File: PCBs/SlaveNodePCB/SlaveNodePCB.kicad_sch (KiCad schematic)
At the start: 0 parts

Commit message: Designed Slave PCB schematic
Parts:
- added C1: 10uF 50v, Capacitor_SMD:C_0805_2012Metric, symbol Device:C
- added C10, C7: 0.1uF, Capacitor_SMD:C_0805_2012Metric, symbol Device:C
- added C2: 22uF 6.3V, Capacitor_SMD:C_0805_2012Metric, symbol Device:C
- added C3: 150pF, Capacitor_SMD:C_0805_2012Metric, symbol Device:C
- added C4: 100nF, Capacitor_SMD:C_0805_2012Metric, symbol Device:C
- added C5, C6, C9: 1uF, Capacitor_SMD:C_0805_2012Metric, symbol Device:C
- added D1: ~, Capacitor_SMD:C_0805_2012Metric, symbol Device:D_Schottky_Small
- added D2: FR107/1N4007, Diode_THT:D_DO-41_SOD81_P12.70mm_Horizontal, symbol Device:D
- added J1: 8P8C, Connector_RJ:RJ45_Ninigi_GE, symbol Connector:8P8C
- added J2: Screw_Terminal_01x02, TerminalBlock_Phoenix:TerminalBlock_Phoenix_PTSM-0,5-2-2,5-V-SMD_1x02-1MP_P2.50mm_Vertical, symbol Connector:Screw_Terminal_01x02
- added J3: Conn_01x04, Connector_PinHeader_2.54mm:PinHeader_1x04_P2.54mm_Vertical, symbol Connector_Generic:Conn_01x04
- added J4: Conn_01x07, Connector_PinHeader_2.54mm:PinHeader_1x07_P2.54mm_Vertical, symbol Connector_Generic:Conn_01x07
- added L1: 15uH, Inductor_SMD:L_6.3x6.3_H3, symbol Device:L
- added MP1584EN1: ~, Package_SO:SO-8_3.9x4.9mm_P1.27mm, symbol PersonalLibrary:MP1584EN
- added Q1: IRLZ44N, Package_TO_SOT_THT:TO-220-3_Vertical, symbol Transistor_FET:IRLZ44N
- added R1: 210k, Resistor_SMD:R_0805_2012Metric, symbol Device:R_Small_US
- added R2: 40.2k, Resistor_SMD:R_0805_2012Metric, symbol Device:R_Small_US
- added R3, R4, R5: 100k, Resistor_SMD:R_0805_2012Metric, symbol Device:R_Small_US
- added R6: 10K, Resistor_SMD:R_0805_2012Metric, symbol Device:R
- added SW1: RST, Button_Switch_THT:SW_PUSH_6mm, symbol Switch:SW_SPST
- added U1: AP2112K-3.3, Package_TO_SOT_SMD:SOT-23-5, symbol Regulator_Linear:AP2112K-3.3
- added U2: MAX485E, Package_SO:SOIC-8_3.9x4.9mm_P1.27mm, symbol Interface_UART:MAX485E
- added U3: STM8S003F3P, Package_SO:TSSOP-20_4.4x6.5mm_P0.65mm, symbol MCU_ST_STM8:STM8S003F3P
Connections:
- new net: C9.1, U3.8 (VCAP)
- new net: MP1584EN1.6 (FREQ), R4.1
- new net: J2.1 (Pin_1), Q1.2 (D)
- new net: C4.2, D1.1 (K), L1.1, MP1584EN1.1 (SW)
- new net: MP1584EN1.2 (EN), R5.2
- new net: C3.1, MP1584EN1.3 (COMP)
- new net: MP1584EN1.4 (FB), R1.1, R2.1
- new net: C4.1, MP1584EN1.8 (BST)
- new net: C3.2, R3.2
- new net +24V: C1.2, D2.1 (K), J1.6, J1.7, J1.8, J2.2 (Pin_2), MP1584EN1.7 (VIN), R5.1
- new net +3.3V: C10.2, C6.1, J3.1 (Pin_1), U1.5 (VOUT), U3.9 (VDD)
- new net +5V: C2.2, C5.1, J4.7 (Pin_7), L1.2, R1.2, R6.1, U1.1 (VIN), U1.3 (EN), U2.8 (VCC)
- new net 485_EN: U2.2 (~{RE}), U2.3 (DE), U3.1 (PD4)
- new net A485: J1.1, U2.6 (A)
- new net A_IN: J4.1 (Pin_1), U3.12 (PB4)
- new net B485: J1.2, U2.7 (B)
- new net GND: C1.1, C10.1, C2.1, C5.2, C6.2, C7.2, C9.2, D1.2 (A), D2.2 (A), J1.3, J1.4, J1.5, J3.2 (Pin_2), J4.6 (Pin_6), MP1584EN1.5 (GND), Q1.3 (S), R2.2, R3.1, R4.2, SW1.1 (A), U1.2 (GND), U2.5 (GND), U3.7 (VSS)
- new net NRST: C7.1, J3.3 (Pin_3), R6.2, SW1.2 (B)
- new net S0: J4.2 (Pin_2), U3.14 (PC4)
- new net S1: J4.3 (Pin_3), U3.15 (PC5)
- new net S2: J4.4 (Pin_4), U3.16 (PC6)
- new net S3: J4.5 (Pin_5), U3.17 (PC7)
- new net SV_SIGNAL: Q1.1 (G), U3.19 (PD2)
- new net SWIM: J3.4 (Pin_4), U3.18 (PD1)
- new net UART_RX: U2.1 (RO), U3.3 (PD6)
- new net UART_TX: U2.4 (DI), U3.2 (PD5)
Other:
- note added: "24V->5V Step Down Switching Regulator"
- note added: "3.3V Fixed LDO"
- note added: "Input Connector"
- note added: "MAX485"
- note added: "Mux Connect"
- note added: "Program"
- note added: "Reset"
- note added: "STM8S003F3"
- note added: "Solenoid Valve Output"

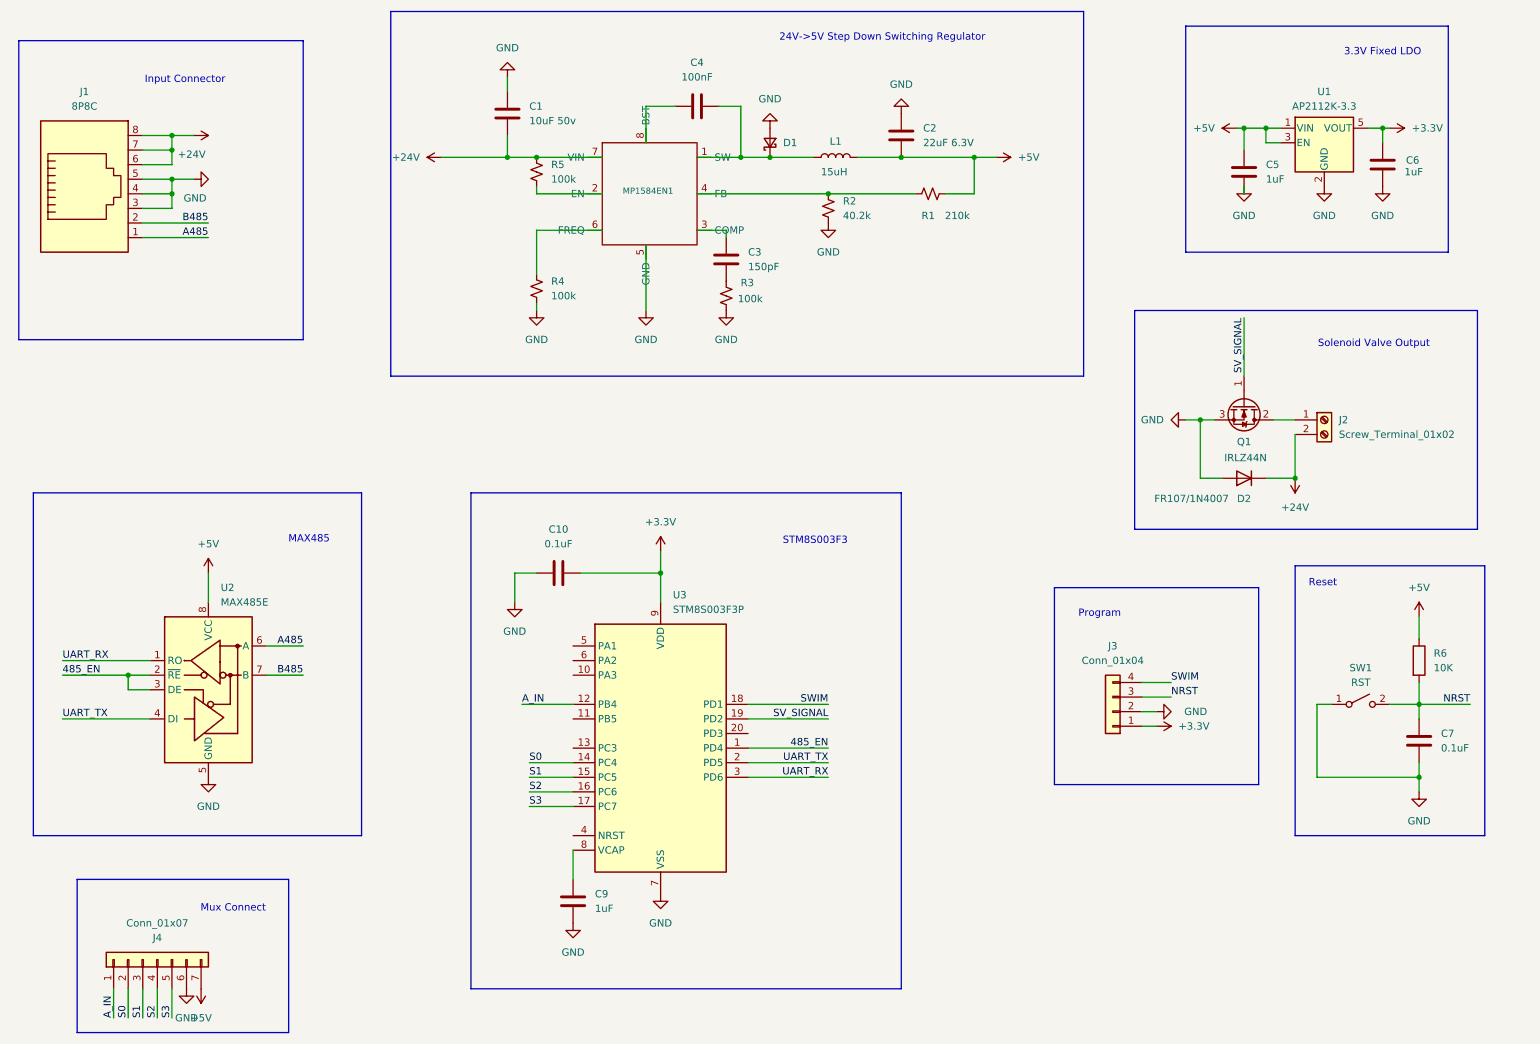
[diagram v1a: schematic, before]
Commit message: First Slave PCB Design Complete
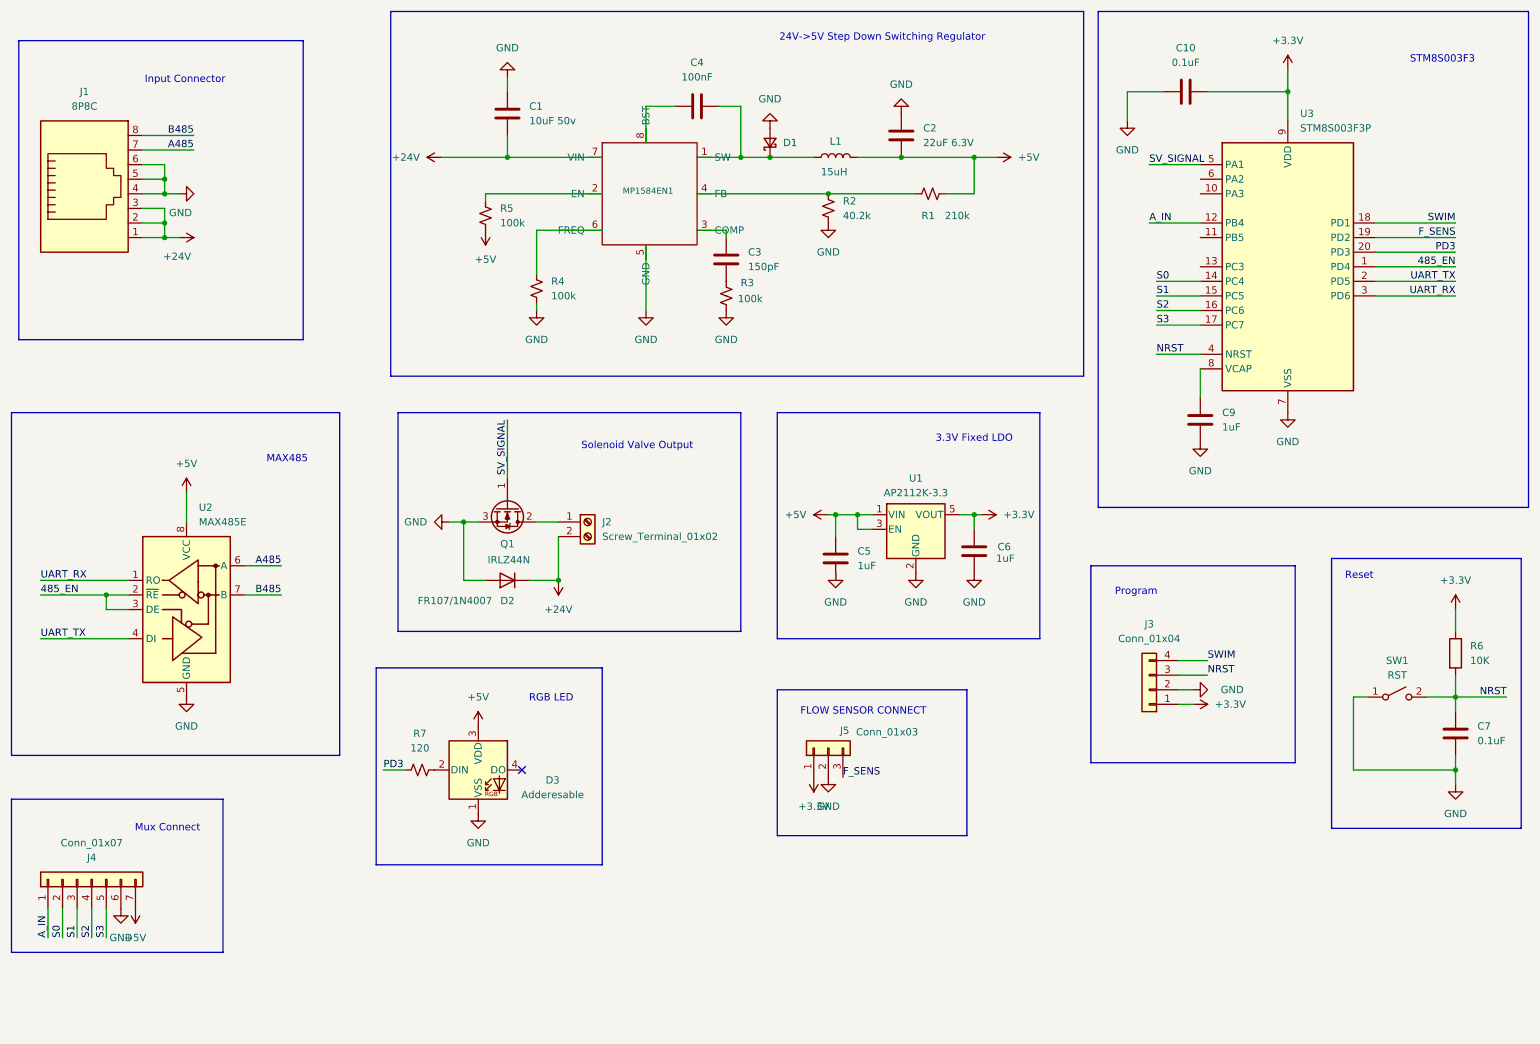
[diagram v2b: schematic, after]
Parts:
- added D3: Adderesable, LED_SMD:LED_Inolux_IN-PI554FCH_PLCC4_5.0x5.0mm_P3.2mm, symbol LED:Inolux_IN-PI554FCH
- added J5: Conn_01x03, Connector_PinHeader_2.54mm:PinHeader_1x03_P2.54mm_Vertical, symbol Connector_Generic:Conn_01x03
- added R7: 120, Resistor_SMD:R_0805_2012Metric, symbol Device:R_Small_US
- D1: footprint Capacitor_SMD:C_0805_2012Metric -> Diode_SMD:D_SMA-SMB_Universal_Handsoldering
- J2: footprint TerminalBlock_Phoenix:TerminalBlock_Phoenix_PTSM-0,5-2-2,5-V-SMD_1x02-1MP_P2.50mm_Vertical -> TerminalBlock_Phoenix:TerminalBlock_Phoenix_PTSM-0,5-2-2.5-V-THR_1x02_P2.50mm_Vertical
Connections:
- net +24V: now also J1.1, J1.2, J1.3; no longer J1.6, J1.7, J1.8, R5.1
- net +3.3V: now also R6.1, J5.1 (Pin_1)
- net +5V: now also R5.1, D3.3 (VDD); no longer R6.1
- net A485: now also J1.7; no longer J1.1
- net B485: now also J1.8; no longer J1.2
- net GND: now also J1.6, D3.1 (VSS), J5.2 (Pin_2); no longer J1.3
- net NRST: now also U3.4 (NRST)
- net SV_SIGNAL: now also U3.5 (PA1); no longer U3.19 (PD2)
- net PD3: now reaches U3.20 (PD3)
- net PD3: now also R7.1
- new net: D3.2 (DIN), R7.2
- new net F_SENS: J5.3 (Pin_3), U3.19 (PD2)
- no-connect marks 0 -> 1
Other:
- note added: "FLOW SENSOR CONNECT"
- note added: "RGB LED"
- moved on the sheet: C10, C5, C6, C7, C9, D2, J2, J3, J4, Q1, R5, R6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

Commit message: Current Slave PCB
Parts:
- J2: footprint TerminalBlock_Phoenix:TerminalBlock_Phoenix_PTSM-0,5-2-2.5-V-THR_1x02_P2.50mm_Vertical -> TerminalBlock_Phoenix:TerminalBlock_Phoenix_MKDS-1,5-2-5.08_1x02_P5.08mm_Horizontal
- L1: footprint Inductor_SMD:L_6.3x6.3_H3 -> Inductor_SMD:L_Changjiang_FNR8040S
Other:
- note added: "VANDIT NARAIN TYAGI NIRAKAAR STUDIOS"
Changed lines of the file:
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@@
 		)
 	)
+	(text "VANDIT NARAIN TYAGI	\nNIRAKAAR STUDIOS"
+		(exclude_from_sim no)
+		(at 205.486 176.022 0)
+		(effects
+			(font
+				(size 2.54 2.54)
+				(italic yes)
+			)
+		)
+	)
 	(text "RGB LED"
 		(exclude_from_sim no)
@@
 			)
 		)
-		(property "Footprint" "TerminalBlock_Phoenix:TerminalBlock_Phoenix_PTSM-0,5-2-2.5-V-THR_1x02_P2.50mm_Vertical"
+		(property "Footprint" "TerminalBlock_Phoenix:TerminalBlock_Phoenix_MKDS-1,5-2-5.08_1x02_P5.08mm_Horizontal"
 			(at 118.11 105.41 0)
 			(effects
@@
 	)
 	(symbol
-		(lib_id "power:GND")
-		(at 240.03 86.36 0)
-		(unit 1)
-		(exclude_from_sim no)
-		(in_bom yes)
-		(on_board yes)
-		(dnp no)
-		(fields_autoplaced yes)
-		(property "Reference" "#PWR027"
-			(at 240.03 92.71 0)
-			(effects
-				(font
-					(size 1.27 1.27)
-				)
-				(hide yes)
-			)
-		)
-		(property "Value" "GND"
-			(at 240.03 91.44 0)
-			(effects
-				(font
-					(size 1.27 1.27)
-				)
-			)
-		)
-		(property "Footprint" ""
-			(at 240.03 86.36 0)
-			(effects
-				(font
-					(size 1.27 1.27)
-				)
-				(hide yes)
-			)
-		)
-		(property "Datasheet" ""
-			(at 240.03 86.36 0)
-			(effects
-				(font
-					(size 1.27 1.27)
-				)
-				(hide yes)
-			)
-		)
-		(property "Description" "Power symbol creates a global label with name \"GND\" , ground"
-			(at 240.03 86.36 0)
-			(effects
-				(font
-					(size 1.27 1.27)
-				)
-				(hide yes)
-			)
-		)
-		(pin "1"
-		)
-		(instances
-			(project "SlaveNodePCB"
-				(path "/1b41d99f-75ff-4da1-9687-8ffd566e2ca3"
-					(reference "#PWR027")
-					(unit 1)
-				)
-			)
-		)
-	)
-	(symbol
 		(lib_id "Switch:SW_SPST")
 		(at 259.08 135.89 0)
@@
 			)
 		)
-		(property "Footprint" "Inductor_SMD:L_6.3x6.3_H3"
+		(property "Footprint" "Inductor_SMD:L_Changjiang_FNR8040S"
 			(at 161.29 41.91 0)
 			(effects
@@
 					(unit 1)
 				)
+			)
+		)
+	)
+	(symbol
+		(lib_id "power:GND")
+		(at 240.03 86.36 0)
+		(unit 1)
+		(exclude_from_sim no)
+		(in_bom yes)
+		(on_board yes)
+		(dnp no)
+		(fields_autoplaced yes)
+		(property "Reference" "#PWR027"
+			(at 240.03 92.71 0)
+			(effects
+				(font
+					(size 1.27 1.27)
+				)
+				(hide yes)
+			)
+		)
+		(property "Value" "GND"
+			(at 240.03 91.44 0)
+			(effects
+				(font
+					(size 1.27 1.27)
+				)
+			)
+		)
+		(property "Footprint" ""
+			(at 240.03 86.36 0)
+			(effects
+				(font
+					(size 1.27 1.27)
+				)
+				(hide yes)
+			)
+		)
+		(property "Datasheet" ""
+			(at 240.03 86.36 0)
+			(effects
+				(font
+					(size 1.27 1.27)
+				)
+				(hide yes)
+			)
+		)
+		(property "Description" "Power symbol creates a global label with name \"GND\" , ground"
+			(at 240.03 86.36 0)
+			(effects
+				(font
+					(size 1.27 1.27)
+				)
+				(hide yes)
+			)
+		)
+		(pin "1"
+		)
+		(instances
+			(project "SlaveNodePCB"
+				(path "/1b41d99f-75ff-4da1-9687-8ffd566e2ca3"
+					(reference "#PWR027")
+					(unit 1)
+				)
